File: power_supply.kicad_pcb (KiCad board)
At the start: 2 copper layers, 110.1 x 73.4 mm, 96 parts, among them J1 USB-IN, J2 USB OUT, Q1 SI4174DY, Q2 SI4463CDY, Q3 SI4463CDY, U1 LM3914, U10 FDC6392S, U11 MCP6041, U2 TPD2E001, U3 MIC2185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

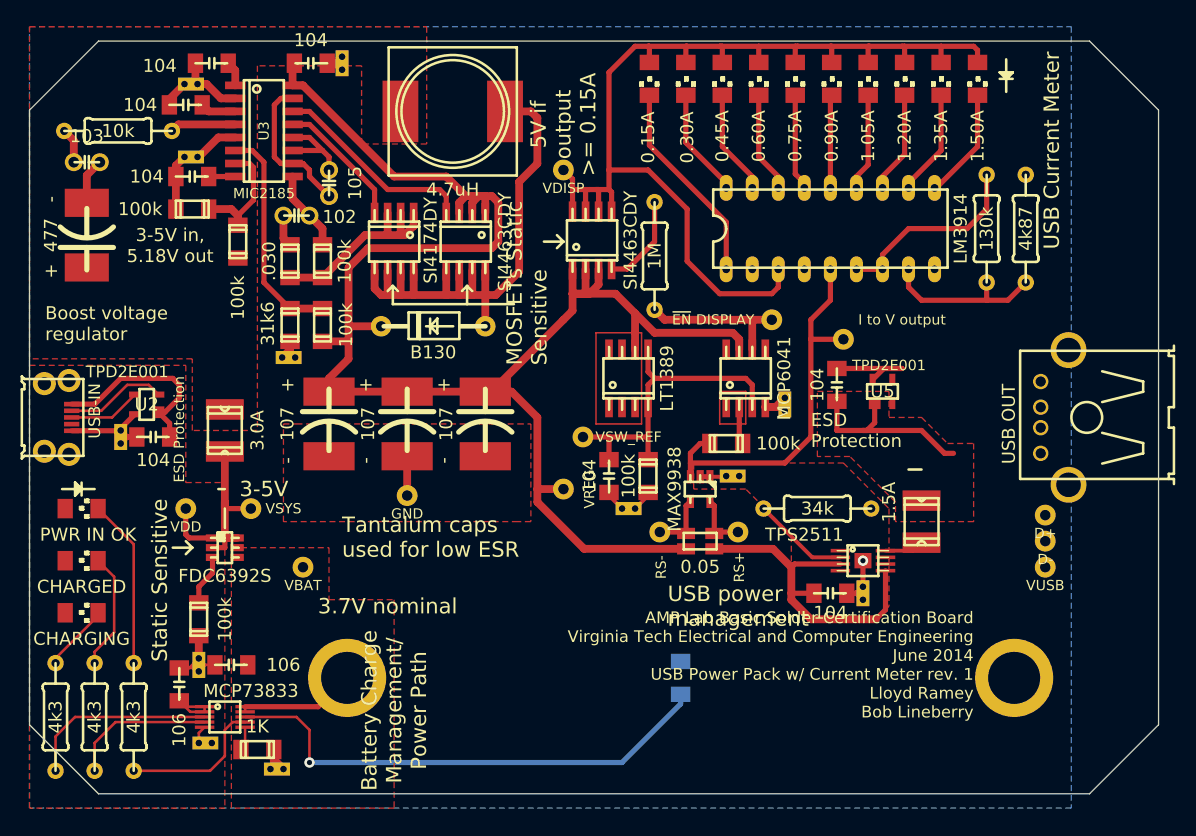
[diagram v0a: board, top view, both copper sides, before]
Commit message: Fixed silkscreen after reshaping
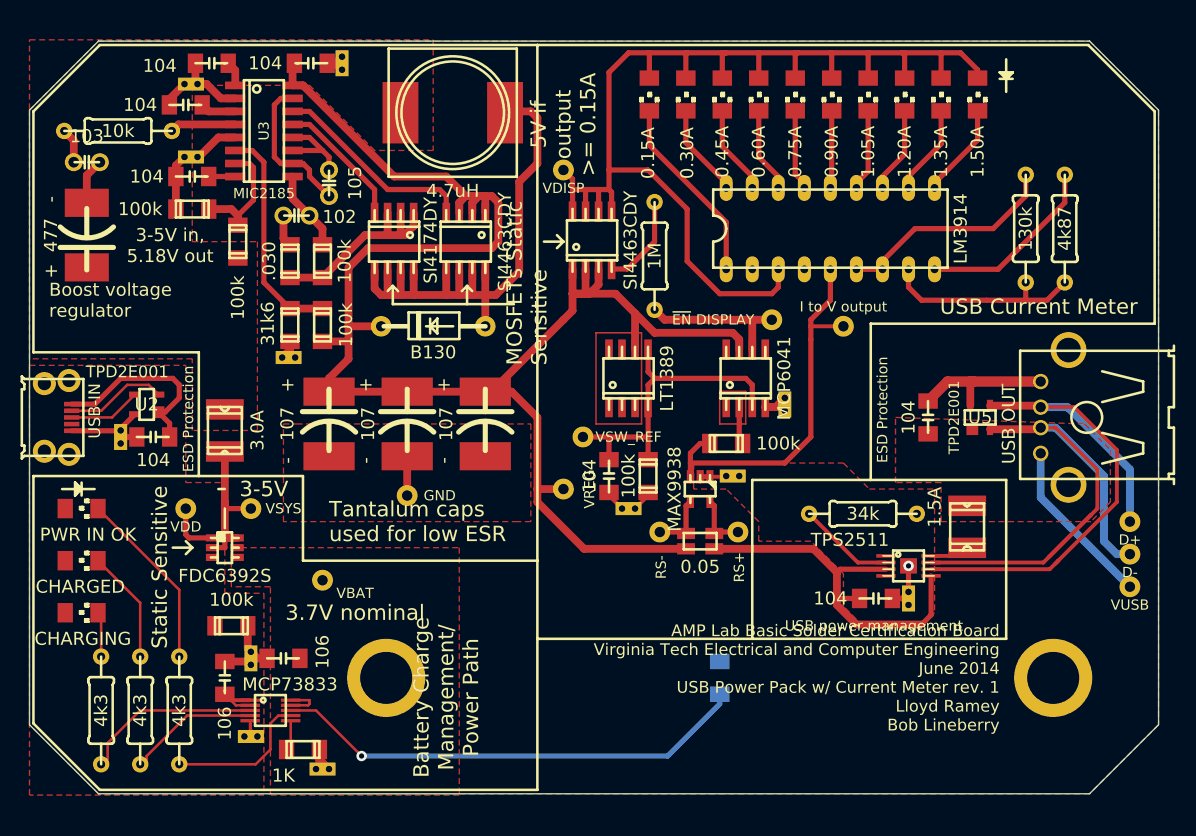
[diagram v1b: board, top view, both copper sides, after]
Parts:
- moved U5 9.86 mm to (245.1, 139.7)
- moved C9 9.44 mm to (240.0, 139.7)
- moved TP2 8.47 mm to (259.7, 156.2)
- moved TP3 8.35 mm to (259.7, 153.0)
- moved TP4 8.28 mm to (259.7, 149.9)
- moved V6 5.12 mm to (174.0, 163.2)
- moved C13 5.12 mm to (177.2, 163.2)
- moved U4 4.49 mm to (175.9, 168.3)
- moved V5 4.49 mm to (174.0, 170.8)
- moved C7 4.49 mm to (171.4, 165.1)
- moved R11 4.49 mm to (167.0, 168.3)
- moved R6 4.49 mm to (163.2, 168.3)
- moved R8 4.49 mm to (159.4, 168.3)
- moved C11 4.47 mm to (234.9, 157.4)
- moved R7 4.47 mm to (233.7, 149.1)
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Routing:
- net /D-: track 0.00 -> 57.8 mm
- net /D+: track 0.00 -> 56.8 mm
- net /VSS: track 96.3 -> 118.6 mm
- net /VDISP: track 106.5 -> 114.5 mm
- net /VBAT: track 11.6 -> 4.09 mm
- net /VDD: track 34.9 -> 29.4 mm
- net /VOUT: track 32.7 -> 37.4 mm
- net N-000003: track 16.2 -> 20.0 mm
- net N-000008: track 49.5 -> 46.7 mm
- net N-000004: track 19.3 -> 22.0 mm
- net N-0000033: track 6.62 -> 4.40 mm
- net N-0000068: track 18.5 -> 16.6 mm
- net N-0000047: track 14.3 -> 12.5 mm
- net N-0000018: track 9.09 -> 7.56 mm
- net N-000005: track 20.1 -> 18.6 mm
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
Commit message: Updated schematic
Added output capacitor onto TPS2511, pull up on EN
Updated board shape
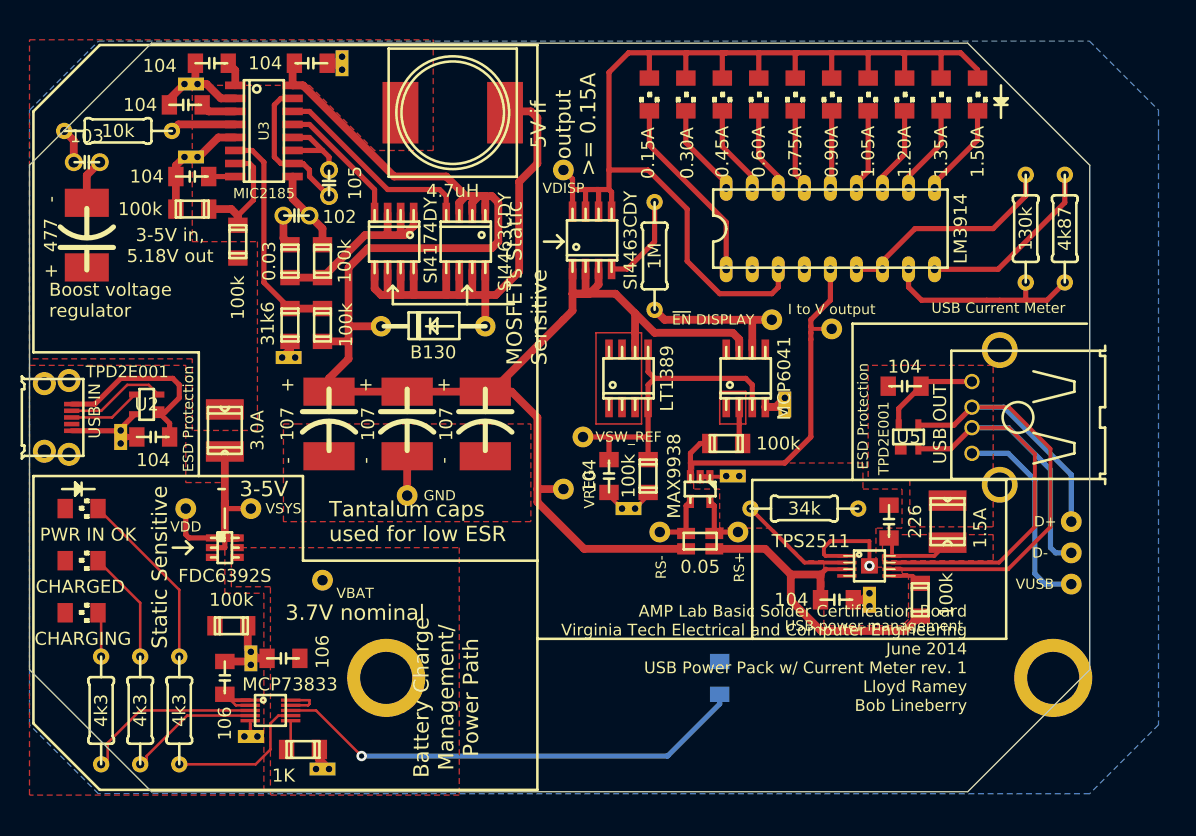
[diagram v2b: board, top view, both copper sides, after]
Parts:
- added C18: 226, c_1206, F.Cu at (236.2, 149.9)
- added R20: 100k, r_1206, F.Cu at (239.3, 157.5)
- R10: value .030 -> 0.03
- moved U5 7.24 mm to (238.1, 141.6)
- moved J2 6.71 mm to (255.8, 139.7)
- moved R7 5.74 mm to (228.0, 148.6)
- moved TP2 5.72 mm to (254.0, 156.0)
- moved TP3 5.72 mm to (254.0, 152.9)
- moved TP4 5.71 mm to (254.0, 149.9)
- moved C11 3.81 mm to (231.1, 157.5)
- moved V11 3.81 mm to (234.3, 157.5)
- moved C9 3.81 mm to (237.7, 136.7), turned to 180 degrees
- moved U6 3.81 mm to (234.3, 154.2)
- moved F2 1.97 mm to (241.9, 149.9)
- moved TP8 1.17 mm to (230.6, 131.1)
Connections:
- U6 pad 5: /VOUT -> N-0000036
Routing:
- net /VUSB: track 3.84 -> 7.82 mm
- net /VOUT: track 37.4 -> 33.6 mm
- net N-0000069: track 16.6 -> 20.3 mm
- net N-0000036: track 0.00 -> 3.05 mm
- net /VSS: track 118.6 -> 121.6 mm
- net /D-: track 57.8 -> 55.0 mm
- net N-0000040: track 9.46 -> 11.6 mm
- net /I_SENSE: track 37.7 -> 36.9 mm
- added copper zone on F.Cu, net /VUSB
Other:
- board size 110.1 x 73.4 mm -> 103.4 x 73 mm

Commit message: Fixed schematic, PCB, and library TPS2511
TPS2511 GND and VCC were switched.
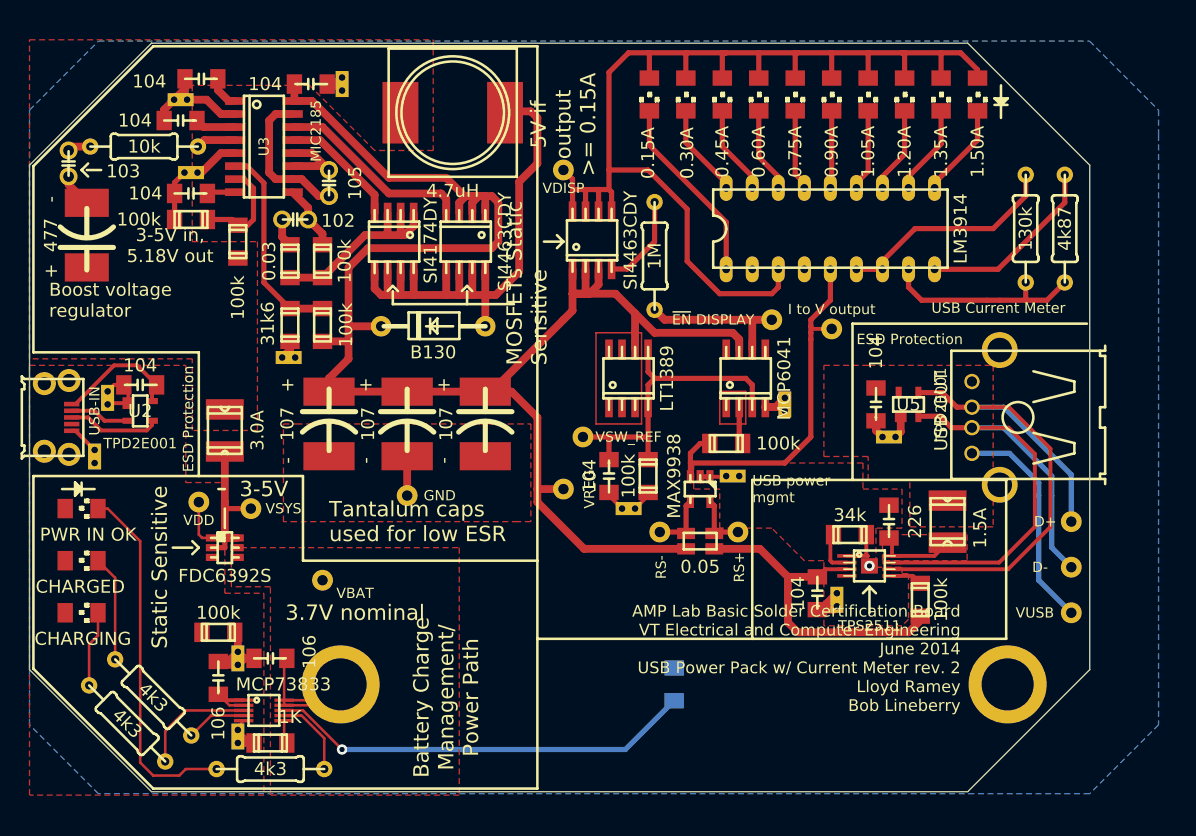
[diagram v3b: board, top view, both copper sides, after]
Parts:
- added V13: DBL_VIA, DBL_VIA, F.Cu at (236.2, 141.6)
- R7: footprint r_pth_2.5x6.5mm -> r_1206
- moved V7 37.7 mm to (158.8, 143.5), turned to 90 degrees
- moved R11 10.6 mm to (175.9, 174.0), turned to 180 degrees
- moved C6 5.24 mm to (163.2, 136.5), turned to 180 degrees
- moved R7 5.12 mm to (232.4, 151.1), turned to 0 degrees
- moved RT1 4.49 mm to (215.3, 165.7)
- moved U7 4.49 mm to (215.3, 165.7)
- moved V4 4.02 mm to (160.0, 137.8)
- moved C9 3.31 mm to (234.9, 138.4), turned to 270 degrees
- moved R12 3.24 mm to (175.9, 171.4), turned to 0 degrees
- moved V11 3.18 mm to (231.1, 157.5)
- moved U5 3.17 mm to (238.1, 138.4)
- moved R5 2.96 mm to (163.6, 113.3)
- moved R8 2.84 mm to (161.9, 169.5), turned to 135 degrees
- moved TP2 2.79 mm to (254.0, 158.8)
- moved C16 2.03 mm to (179.8, 107.2)
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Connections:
- net N-0000050 renamed /VSYS_PROTECTED
- C6 pad 1: /VDD -> /VSS
- C6 pad 2: /VSS -> /VDD
- C9 pad 1: N-0000069 -> /VSS
- C9 pad 2: /VSS -> /VUSB_PROTECTED
- F2 pad 1: N-0000069 -> /VUSB_PROTECTED
- J2 pad 1: N-0000069 -> /VUSB_PROTECTED
- TP2 pad 1: N-0000069 -> /VUSB_PROTECTED
- U2 pad 1: /VDD -> /VSS
- U2 pad 4: /VSS -> /VDD
- U5 pad 1: N-0000069 -> /VSS
- U5 pad 4: /VSS -> /VUSB_PROTECTED
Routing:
- net /VUSB_PROTECTED: track 0.00 -> 21.7 mm
- net N-0000069: track 20.3 -> 0.00 mm
- net N-0000013: track 17.7 -> 35.3 mm
- net /VBAT: track 4.09 -> 17.2 mm
- net /VSS: track 121.6 -> 112.0 mm
- net N-0000012: track 11.6 -> 4.35 mm
- net /VDD: track 29.4 -> 22.7 mm
- net N-0000047: track 12.5 -> 5.91 mm
- net N-000002: track 13.7 -> 7.83 mm
- net N-0000061: track 17.3 -> 11.5 mm
- net N-0000014: track 46.7 -> 41.6 mm
- net N-0000034: track 9.90 -> 5.93 mm
- net N-000009: track 4.40 -> 7.44 mm
- net N-0000051: track 6.44 -> 3.90 mm
- net N-0000035: track 7.09 -> 9.00 mm
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- added copper zone on F.Cu, net /VUSB_PROTECTED
- removed copper zone on F.Cu, net N-0000069
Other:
- board text added: "AMP Lab Basic Solder Certification Board VT Electrical and Computer Engineering June 2014 USB Power Pack w/ Current Meter rev. 2 Lloyd Ramey Bob Lineberry"
- board text added: "USB power mgmt"
- board text removed: "AMP Lab Basic Solder Certification Board Virginia Tech Electrical and Computer Engineering June 2014 USB Power Pack w/ Current Meter rev. 1 Lloyd Ramey Bob Lineberry"
- board text removed: "USB power management"

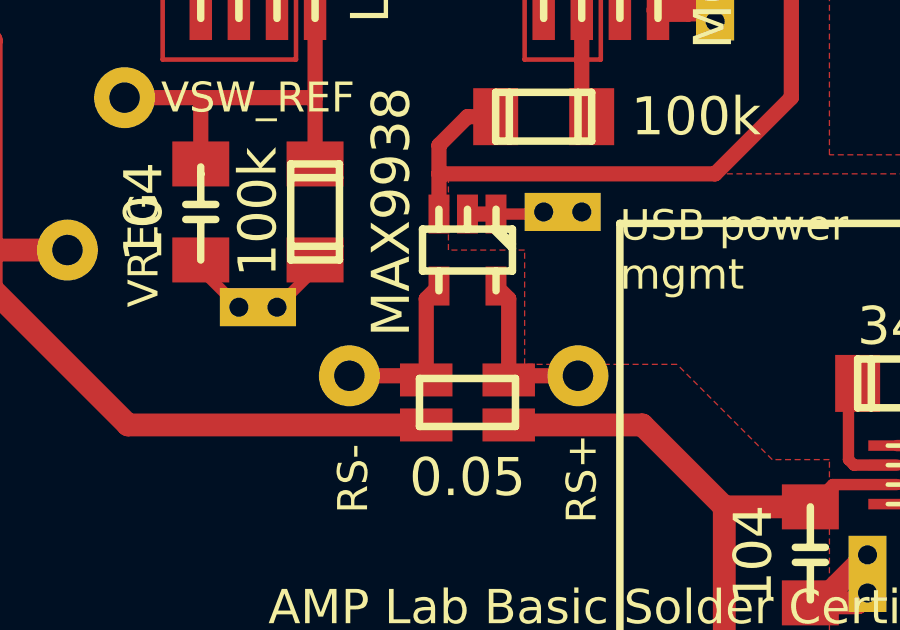
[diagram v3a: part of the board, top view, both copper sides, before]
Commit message: Fixed MAX9938
RS+/RS- reversed
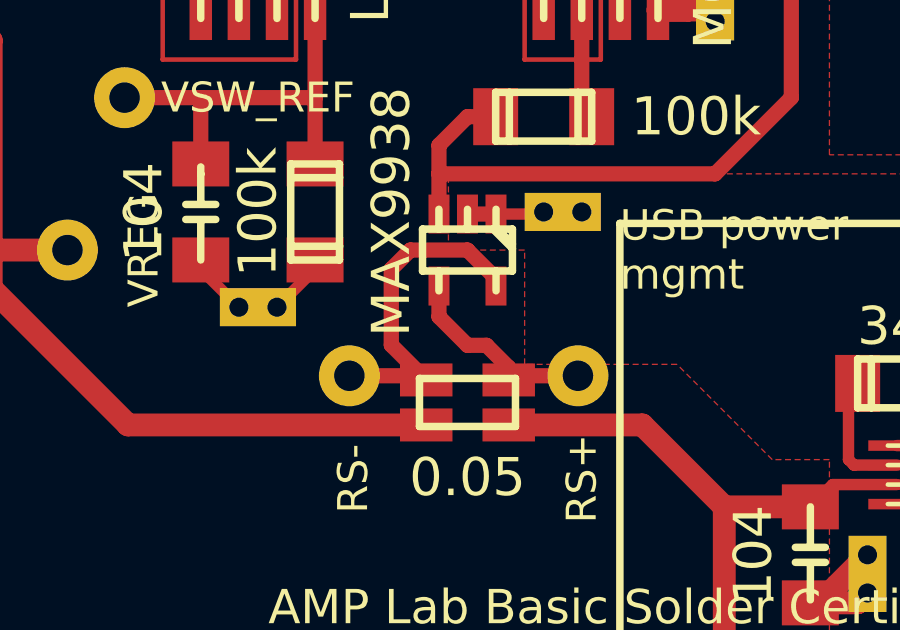
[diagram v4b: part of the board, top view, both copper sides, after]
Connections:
- R17 pad V1: N-0000028 -> N-0000029
- R17 pad V2: N-0000038 -> N-0000032
- TP10 pad 1: N-0000038 -> N-0000032
- TP9 pad 1: N-0000028 -> N-0000029
- U9 pad 4: N-0000028 -> N-0000032
- U9 pad 5: N-0000038 -> N-0000029
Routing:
- net N-0000029: track 0.00 -> 11.2 mm
- net N-0000032: track 0.00 -> 6.83 mm
- net N-0000028: track 5.93 -> 0.00 mm
- net N-0000038: track 5.67 -> 0.00 mm

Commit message: Fixed test points for RS+/-
Reversed
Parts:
- moved TP10 7.62 mm to (213.9, 150.9)
- moved TP9 7.62 mm to (221.5, 150.9)
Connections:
- R17 pad V1: N-0000029 -> N-0000032
- R17 pad V2: N-0000032 -> N-0000029
- U9 pad 4: N-0000032 -> N-0000029
- U9 pad 5: N-0000029 -> N-0000032
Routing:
- net N-0000032: track 6.83 -> 11.2 mm
- net N-0000029: track 11.2 -> 6.83 mm
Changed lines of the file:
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@@
   )
   (setup
-    (last_trace_width 0.508)
+    (last_trace_width 0.254)
     (user_trace_width 0.1524)
     (user_trace_width 0.381)
@@
     (pad V1 smd rect (at -1.375 -0.75) (size 1.75 1.1)
       (layers F.Cu F.Paste F.Mask)
-      (net 31 N-0000029)
+      (net 32 N-0000032)
     )
     (pad V2 smd rect (at 1.375 -0.75) (size 1.75 1.1)
       (layers F.Cu F.Paste F.Mask)
-      (net 32 N-0000032)
+      (net 31 N-0000029)
     )
     (pad I2 smd rect (at 1.375 0.75) (size 1.75 1.1)
@@
   )
   (module TP (layer F.Cu)
-    (at 221.488 150.876)
+    (at 213.868 150.876)
     (fp_text reference TP10 (at 0 -1.778) (layer F.SilkS) hide
       (effects (font (size 1 1) (thickness 0.15)))
@@
   )
   (module TP (layer F.Cu)
-    (at 213.868 150.876)
+    (at 221.488 150.876)
     (fp_text reference TP9 (at 0 -1.778) (layer F.SilkS) hide
       (effects (font (size 1 1) (thickness 0.15)))
@@
     (pad 4 smd rect (at 0.95 -1.2 180) (size 0.7 1.3)
       (layers F.Cu F.Paste F.Mask)
-      (net 32 N-0000032)
+      (net 31 N-0000029)
     )
     (pad 5 smd rect (at -0.95 -1.2 180) (size 0.7 1.3)
       (layers F.Cu F.Paste F.Mask)
-      (net 31 N-0000029)
+      (net 32 N-0000032)
     )
     (model walter\smd_trans\sot23-6.wrl
@@
   (segment (start 222.885 116.205) (end 219.964 113.284) (width 0.508) (layer F.Cu) (net 30))
   (segment (start 219.964 113.284) (end 219.964 109.804) (width 0.508) (layer F.Cu) (net 30))
-  (segment (start 218.755 147.885) (end 218.755 147.635) (width 0.508) (layer F.Cu) (net 31) (status C00000))
-  (segment (start 215.265 149.85) (end 216.43 151.015) (width 0.508) (layer F.Cu) (net 31) (status 800000))
-  (segment (start 215.265 147.32) (end 215.265 149.85) (width 0.508) (layer F.Cu) (net 31))
-  (segment (start 215.9 146.685) (end 215.265 147.32) (width 0.508) (layer F.Cu) (net 31))
-  (segment (start 217.805 146.685) (end 215.9 146.685) (width 0.508) (layer F.Cu) (net 31))
-  (segment (start 218.755 147.635) (end 217.805 146.685) (width 0.508) (layer F.Cu) (net 31) (status 400000))
-  (segment (start 213.868 150.876) (end 216.291 150.876) (width 0.508) (layer F.Cu) (net 31) (status 30))
-  (segment (start 216.291 150.876) (end 216.43 151.015) (width 0.508) (layer F.Cu) (net 31) (status 30))
-  (segment (start 216.855 147.885) (end 216.855 148.91) (width 0.508) (layer F.Cu) (net 32) (status 400000))
-  (segment (start 219.18 150.6) (end 219.18 151.015) (width 0.508) (layer F.Cu) (net 32) (status C00000))
-  (segment (start 218.44 149.86) (end 219.18 150.6) (width 0.508) (layer F.Cu) (net 32) (status 800000))
-  (segment (start 217.805 149.86) (end 218.44 149.86) (width 0.508) (layer F.Cu) (net 32))
-  (segment (start 216.855 148.91) (end 217.805 149.86) (width 0.508) (layer F.Cu) (net 32))
-  (segment (start 221.488 150.876) (end 219.319 150.876) (width 0.508) (layer F.Cu) (net 32) (status 30))
-  (segment (start 219.319 150.876) (end 219.18 151.015) (width 0.508) (layer F.Cu) (net 32) (status 30))
+  (segment (start 216.855 147.885) (end 216.855 148.91) (width 0.508) (layer F.Cu) (net 31))
+  (segment (start 219.18 150.6) (end 219.18 151.015) (width 0.508) (layer F.Cu) (net 31))
+  (segment (start 218.44 149.86) (end 219.18 150.6) (width 0.508) (layer F.Cu) (net 31))
+  (segment (start 217.805 149.86) (end 218.44 149.86) (width 0.508) (layer F.Cu) (net 31))
+  (segment (start 216.855 148.91) (end 217.805 149.86) (width 0.508) (layer F.Cu) (net 31))
+  (segment (start 221.488 150.876) (end 219.319 150.876) (width 0.508) (layer F.Cu) (net 31) (status 30))
+  (segment (start 219.319 150.876) (end 219.18 151.015) (width 0.508) (layer F.Cu) (net 31) (status 30))
+  (segment (start 213.868 150.876) (end 216.291 150.876) (width 0.508) (layer F.Cu) (net 32) (status 30))
+  (segment (start 218.755 147.885) (end 218.755 147.635) (width 0.508) (layer F.Cu) (net 32))
+  (segment (start 215.265 149.85) (end 216.43 151.015) (width 0.508) (layer F.Cu) (net 32))
+  (segment (start 215.265 147.32) (end 215.265 149.85) (width 0.508) (layer F.Cu) (net 32))
+  (segment (start 215.9 146.685) (end 215.265 147.32) (width 0.508) (layer F.Cu) (net 32))
+  (segment (start 217.805 146.685) (end 215.9 146.685) (width 0.508) (layer F.Cu) (net 32))
+  (segment (start 218.755 147.635) (end 217.805 146.685) (width 0.508) (layer F.Cu) (net 32))
+  (segment (start 216.291 150.876) (end 216.43 151.015) (width 0.508) (layer F.Cu) (net 32) (status 30))
   (segment (start 236.515 155.153) (end 238.541 155.153) (width 0.381) (layer F.Cu) (net 33))
   (segment (start 238.541 155.153) (end 239.268 155.88) (width 0.381) (layer F.Cu) (net 33))
